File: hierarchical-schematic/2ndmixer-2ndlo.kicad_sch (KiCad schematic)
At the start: 54 parts, among them J201 110.7 MHz In, J202 Conn_01x02, J203 2nd Mixer Out, Q201 2N5179, Q202 2N5179, T201 Bifilar_Transformer, U201 MAV-11, U202 TUF-1H+, Y201 100MHz

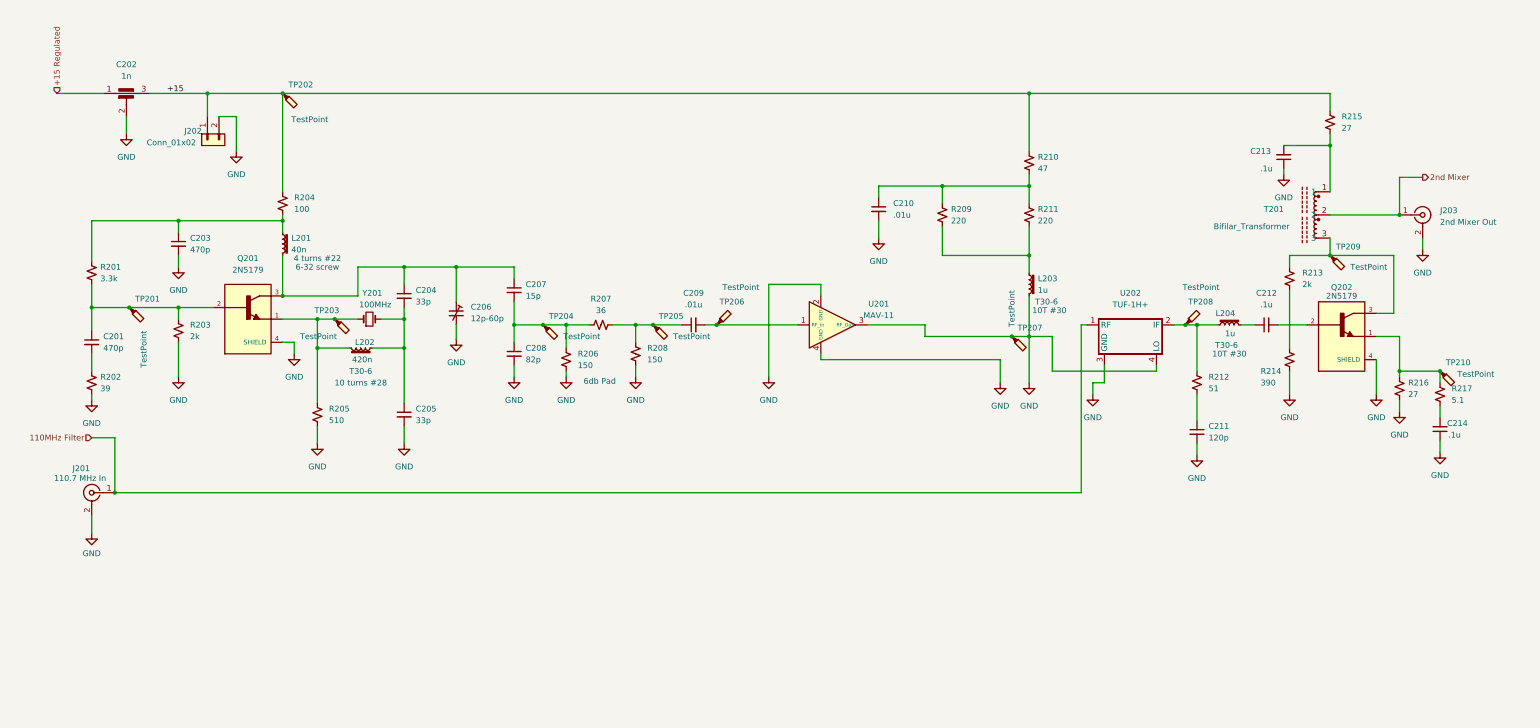
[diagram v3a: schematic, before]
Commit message: Fixes to 2ndmixer-2ndlo and vco-1stmixer
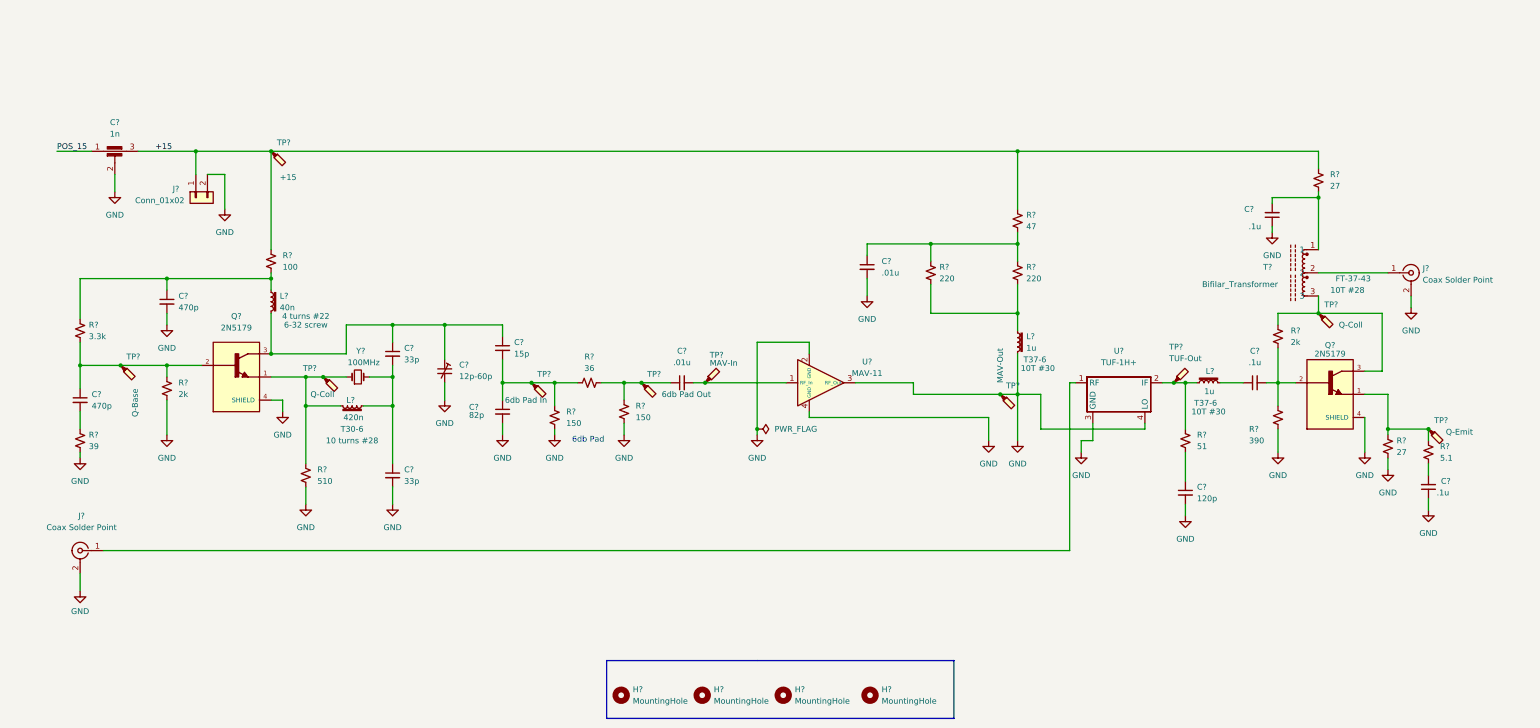
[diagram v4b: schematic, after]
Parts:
- removed C201, C203: 470p, Capacitor_THT:C_Disc_D5.0mm_W2.5mm_P5.00mm, symbol Device:C_Small
- removed C202: 1n, 2ndmixer-2ndlo:DSS1NB32A102Q91A, symbol Device:C_Feedthrough
- removed C204, C205: 33p, Capacitor_THT:C_Disc_D5.0mm_W2.5mm_P5.00mm, symbol Device:C_Small
- removed C206: 12p-60p, 2ndmixer-2ndlo:GKG60015, symbol Device:C_Trim_Small
- removed C207: 15p, Capacitor_THT:C_Disc_D5.0mm_W2.5mm_P5.00mm, symbol Device:C_Small
- removed C208: 82p, Capacitor_THT:C_Disc_D5.0mm_W2.5mm_P5.00mm, symbol Device:C_Small
- removed C209, C210: .01u, Capacitor_THT:C_Disc_D5.0mm_W2.5mm_P5.00mm, symbol Device:C_Small
- removed C211: 120p, Capacitor_THT:C_Disc_D5.0mm_W2.5mm_P5.00mm, symbol Device:C_Small
- removed C212, C213, C214: .1u, Capacitor_THT:C_Disc_D5.0mm_W2.5mm_P5.00mm, symbol Device:C_Small
- removed J201: 110.7 MHz In, Connector_Wire:SolderWire-0.5sqmm_1x02_P4.6mm_D0.9mm_OD2.1mm, symbol Connector:Conn_Coaxial
- removed J202: Conn_01x02, 2ndmixer-2ndlo:691103110002, symbol Connector_Generic:Conn_01x02
- removed J203: 2nd Mixer Out, Connector_Wire:SolderWire-0.5sqmm_1x02_P4.6mm_D0.9mm_OD2.1mm, symbol Connector:Conn_Coaxial
- removed L201: 40n, Inductor_THT:L_Toroid_Vertical_L13.0mm_W6.5mm_P5.60mm, symbol Device:L_Iron_Small
- removed L202: 420n, Inductor_THT:L_Toroid_Vertical_L13.0mm_W6.5mm_P5.60mm, symbol Device:L_Iron_Small
- removed L203, L204: 1u, Inductor_THT:L_Toroid_Vertical_L13.0mm_W6.5mm_P5.60mm, symbol Device:L_Iron_Small
- removed Q201, Q202: 2N5179, TO127P584H533-4N, symbol spectrum analyzer:2N5179
- removed R201: 3.3k, Resistor_THT:R_Axial_DIN0207_L6.3mm_D2.5mm_P7.62mm_Horizontal, symbol Device:R_Small_US
- removed R202: 39, Resistor_THT:R_Axial_DIN0207_L6.3mm_D2.5mm_P7.62mm_Horizontal, symbol Device:R_Small_US
- removed R203, R213: 2k, Resistor_THT:R_Axial_DIN0207_L6.3mm_D2.5mm_P7.62mm_Horizontal, symbol Device:R_Small_US
- removed R204: 100, Resistor_THT:R_Axial_DIN0207_L6.3mm_D2.5mm_P7.62mm_Horizontal, symbol Device:R_Small_US
- removed R205: 510, Resistor_THT:R_Axial_DIN0207_L6.3mm_D2.5mm_P7.62mm_Horizontal, symbol Device:R_Small_US
- removed R206, R208: 150, Resistor_THT:R_Axial_DIN0207_L6.3mm_D2.5mm_P7.62mm_Horizontal, symbol Device:R_Small_US
- removed R207: 36, Resistor_THT:R_Axial_DIN0207_L6.3mm_D2.5mm_P7.62mm_Horizontal, symbol Device:R_Small_US
- removed R209, R211: 220, Resistor_THT:R_Axial_DIN0207_L6.3mm_D2.5mm_P7.62mm_Horizontal, symbol Device:R_Small_US
- removed R210: 47, Resistor_THT:R_Axial_DIN0207_L6.3mm_D2.5mm_P7.62mm_Horizontal, symbol Device:R_Small_US
- removed R212: 51, Resistor_THT:R_Axial_DIN0207_L6.3mm_D2.5mm_P7.62mm_Horizontal, symbol Device:R_Small_US
- removed R214: 390, Resistor_THT:R_Axial_DIN0207_L6.3mm_D2.5mm_P7.62mm_Horizontal, symbol Device:R_Small_US
- removed R215, R216: 27, Resistor_THT:R_Axial_DIN0207_L6.3mm_D2.5mm_P7.62mm_Horizontal, symbol Device:R_Small_US
- removed R217: 5.1, Resistor_THT:R_Axial_DIN0207_L6.3mm_D2.5mm_P7.62mm_Horizontal, symbol Device:R_Small_US
- removed T201: Bifilar_Transformer, Transformer_THT:Autotransformer_Toroid_1Tap_Horizontal_D10.5mm_Amidon-T37, symbol spectrum analyzer:Bifilar_Transformer
- removed TP201, TP202, TP203, TP204, TP205, TP206, TP207, TP208, TP209, TP210: TestPoint, TestPoint:TestPoint_Pad_1.0x1.0mm, symbol Connector:TestPoint_Probe
- removed U201: MAV-11, 2ndmixer-2ndlo:MAV-11BSM&plus_, symbol spectrum analyzer:MAV-11
- removed U202: TUF-1H+, 2ndmixer-2ndlo:TUF-1H, symbol spectrum analyzer:TUF-1H+
- removed Y201: 100MHz, Crystal:Crystal_HC49-U_Vertical, symbol Device:Crystal_Small
- added C? (x3): .1u, Capacitor_THT:C_Disc_D5.0mm_W2.5mm_P5.00mm, symbol Device:C_Small
- added C?: 15p, Capacitor_THT:C_Disc_D5.0mm_W2.5mm_P5.00mm, symbol Device:C_Small
- added C?: 120p, Capacitor_THT:C_Disc_D5.0mm_W2.5mm_P5.00mm, symbol Device:C_Small
- added C? (x2): 33p, Capacitor_THT:C_Disc_D5.0mm_W2.5mm_P5.00mm, symbol Device:C_Small
- added C?: 1n, 2ndmixer-2ndlo:DSS1NB32A102Q91A, symbol Device:C_Feedthrough
- added C?: 82p, Capacitor_THT:C_Disc_D5.0mm_W2.5mm_P5.00mm, symbol Device:C_Small
- added C?: 12p-60p, 2ndmixer-2ndlo:GKG60015, symbol Device:C_Trim_Small
- added C? (x2): 470p, Capacitor_THT:C_Disc_D5.0mm_W2.5mm_P5.00mm, symbol Device:C_Small
- added C? (x2): .01u, Capacitor_THT:C_Disc_D5.0mm_W2.5mm_P5.00mm, symbol Device:C_Small
- added H? (x4): MountingHole, MountingHole:MountingHole_3.2mm_M3, symbol Mechanical:MountingHole
- added J? (x2): Coax Solder Point, Connector_Wire:SolderWire-0.5sqmm_1x02_P4.6mm_D0.9mm_OD2.1mm, symbol Connector:Conn_Coaxial
- added J?: Conn_01x02, 2ndmixer-2ndlo:691103110002, symbol Connector_Generic:Conn_01x02
- added L?: 40n, Inductor_THT:L_Toroid_Vertical_L13.0mm_W6.5mm_P5.60mm, symbol Device:L_Iron_Small
- added L?: 420n, Inductor_THT:L_Toroid_Vertical_L13.0mm_W6.5mm_P5.60mm, symbol Device:L_Iron_Small
- added L? (x2): 1u, Inductor_THT:L_Toroid_Vertical_L13.0mm_W6.5mm_P5.60mm, symbol Device:L_Iron_Small
- added Q?: 2N5179, TO127P584H533-4N, symbol spectrum_analyzer:2N5179
- added Q?: 2N5179, 2ndmixer-2ndlo:TO127P584H533-4N, symbol 2ndmixer-2ndlo:2N5179
- added R?: 100, Resistor_THT:R_Axial_DIN0207_L6.3mm_D2.5mm_P7.62mm_Horizontal, symbol Device:R_Small_US
- added R?: 47, Resistor_THT:R_Axial_DIN0207_L6.3mm_D2.5mm_P7.62mm_Horizontal, symbol Device:R_Small_US
- added R? (x2): 220, Resistor_THT:R_Axial_DIN0207_L6.3mm_D2.5mm_P7.62mm_Horizontal, symbol Device:R_Small_US
- added R? (x2): 27, Resistor_THT:R_Axial_DIN0207_L6.3mm_D2.5mm_P7.62mm_Horizontal, symbol Device:R_Small_US
- added R? (x2): 150, Resistor_THT:R_Axial_DIN0207_L6.3mm_D2.5mm_P7.62mm_Horizontal, symbol Device:R_Small_US
- added R? (x2): 2k, Resistor_THT:R_Axial_DIN0207_L6.3mm_D2.5mm_P7.62mm_Horizontal, symbol Device:R_Small_US
- added R?: 51, Resistor_THT:R_Axial_DIN0207_L6.3mm_D2.5mm_P7.62mm_Horizontal, symbol Device:R_Small_US
- added R?: 390, Resistor_THT:R_Axial_DIN0207_L6.3mm_D2.5mm_P7.62mm_Horizontal, symbol Device:R_Small_US
- added R?: 3.3k, Resistor_THT:R_Axial_DIN0207_L6.3mm_D2.5mm_P7.62mm_Horizontal, symbol Device:R_Small_US
- added R?: 36, Resistor_THT:R_Axial_DIN0207_L6.3mm_D2.5mm_P7.62mm_Horizontal, symbol Device:R_Small_US
- added R?: 510, Resistor_THT:R_Axial_DIN0207_L6.3mm_D2.5mm_P7.62mm_Horizontal, symbol Device:R_Small_US
- added R?: 39, Resistor_THT:R_Axial_DIN0207_L6.3mm_D2.5mm_P7.62mm_Horizontal, symbol Device:R_Small_US
- added R?: 5.1, Resistor_THT:R_Axial_DIN0207_L6.3mm_D2.5mm_P7.62mm_Horizontal, symbol Device:R_Small_US
- added T?: Bifilar_Transformer, Transformer_THT:Autotransformer_Toroid_1Tap_Horizontal_D10.5mm_Amidon-T37, symbol spectrum_analyzer:Bifilar_Transformer
- added TP? (x2): Q-Coll, TestPoint:TestPoint_Pad_1.0x1.0mm, symbol Connector:TestPoint_Probe
- added TP?: 6db Pad Out, TestPoint:TestPoint_Pad_1.0x1.0mm, symbol Connector:TestPoint_Probe
- added TP?: MAV-Out, TestPoint:TestPoint_Pad_1.0x1.0mm, symbol Connector:TestPoint_Probe
- added TP?: Q-Emit, TestPoint:TestPoint_Pad_1.0x1.0mm, symbol Connector:TestPoint_Probe
- added TP?: +15, TestPoint:TestPoint_Pad_1.0x1.0mm, symbol Connector:TestPoint_Probe
- added TP?: 6db Pad In, TestPoint:TestPoint_Pad_1.0x1.0mm, symbol Connector:TestPoint_Probe
- added TP?: Q-Base, TestPoint:TestPoint_Pad_1.0x1.0mm, symbol Connector:TestPoint_Probe
- added TP?: TUF-Out, TestPoint:TestPoint_Pad_1.0x1.0mm, symbol Connector:TestPoint_Probe
- added TP?: MAV-In, TestPoint:TestPoint_Pad_1.0x1.0mm, symbol Connector:TestPoint_Probe
- added U?: MAV-11, 2ndmixer-2ndlo:MAV-11BSM&plus_, symbol spectrum_analyzer:MAV-11
- added U?: TUF-1H+, 2ndmixer-2ndlo:TUF-1H, symbol spectrum_analyzer:TUF-1H+
- added Y?: 100MHz, Crystal:Crystal_HC49-U_Vertical, symbol Device:Crystal_Small
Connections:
- net +15: now also C?.3, J?.1 (Pin_1), R?.1, R?.1, R?.1, TP?.1
- net GND: now also C?.1, C?.1, C?.2, C?.2, C?.2, C?.2, C?.2, C?.2, C?.2, J?.2 (Ext), J?.2 (Ext), J?.2 (Pin_2), L?.2, Q?.4 (SHIELD), Q?.4 (SHIELD), R?.2, R?.2, R?.2, R?.2, R?.2, R?.2, R?.2, TP?.1, U?.2 (GND), U?.3 (GND), U?.3 (RF_Out), U?.4 (GND), U?.4 (LO)
- new net: C?.2, R?.2, T?.1
- new net: Q?.3, R?.1, T?.3, TP?.1
- new net: C?.1, C?.1, C?.1, L?.2, Q?.3
- new net: C?.1, C?.2, R?.1, R?.1, TP?.1
- new net: C?.1, R?.1, R?.2, TP?.1
- new net: L?.2, Q?.1, R?.1, TP?.1, Y?.1
- new net: C?.1, L?.1, R?.1, R?.2
- new net: C?.1, R?.2
- new net: C?.1, R?.1, R?.1, R?.2
- new net: C?.1, C?.2, L?.1, Y?.2
- new net: C?.1, L?.2
- new net: C?.2, Q?.2, R?.1, R?.2
- new net: L?.1, R?.2, R?.2
- new net: Q?.1, R?.1, R?.1, TP?.1
- new net: C?.2, TP?.1, U?.1 (RF_In)
- new net: J?.1 (In), T?.2
- new net: J?.1 (In), U?.1 (RF)
- new net: L?.1, R?.1, TP?.1, U?.2 (IF)
- new net: C?.1, Q?.2, R?.1, R?.2, TP?.1
- new net: C?.2, R?.2
- new net: C?.2, R?.1
- new net POS_15: C?.1
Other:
- title: (none) -> 2nd Mixer and Second LO

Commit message: v7 conversion
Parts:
- J? (x2): Spice_Model Conn_Coaxial -> (none); Spice_Netlist_Enabled N -> (none); Spice_Primitive J -> (none)
- J?: Spice_Model Conn_01x02 -> (none); Spice_Netlist_Enabled N -> (none); Spice_Primitive J -> (none)
- Q? (x2): Spice_Lib_File 2ndmixer-2ndlo-spice\2N5179.LIB -> (none); Spice_Model 2N5179 -> (none); Spice_Netlist_Enabled Y -> (none); Spice_Primitive Q -> (none)
- TP? (x2): value Q-Coll -> ${SIM.PARAMS}; Spice_Netlist_Enabled N -> (none)
- TP?: value 6db Pad Out -> ${SIM.PARAMS}; Spice_Netlist_Enabled N -> (none)
- TP?: value MAV-Out -> ${SIM.PARAMS}; Spice_Netlist_Enabled N -> (none)
- TP?: value Q-Emit -> ${SIM.PARAMS}; Spice_Netlist_Enabled N -> (none)
- TP?: value +15 -> ${SIM.PARAMS}; Spice_Netlist_Enabled N -> (none)
- TP?: value 6db Pad In -> ${SIM.PARAMS}; Spice_Netlist_Enabled N -> (none)
- TP?: value Q-Base -> ${SIM.PARAMS}; Spice_Netlist_Enabled N -> (none)
- TP?: value TUF-Out -> ${SIM.PARAMS}; Spice_Netlist_Enabled N -> (none)
- TP?: value MAV-In -> ${SIM.PARAMS}; Spice_Netlist_Enabled N -> (none)

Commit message: 2ndmixer-2ndlo rev 1
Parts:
- removed C? (x3): .1u, Capacitor_THT:C_Disc_D5.0mm_W2.5mm_P5.00mm, symbol Device:C_Small
- removed C?: 15p, Capacitor_THT:C_Disc_D5.0mm_W2.5mm_P5.00mm, symbol Device:C_Small
- removed C?: 120p, Capacitor_THT:C_Disc_D5.0mm_W2.5mm_P5.00mm, symbol Device:C_Small
- removed C? (x2): 33p, Capacitor_THT:C_Disc_D5.0mm_W2.5mm_P5.00mm, symbol Device:C_Small
- removed C?: 1n, 2ndmixer-2ndlo:DSS1NB32A102Q91A, symbol Device:C_Feedthrough
- removed C?: 82p, Capacitor_THT:C_Disc_D5.0mm_W2.5mm_P5.00mm, symbol Device:C_Small
- removed C?: 12p-60p, 2ndmixer-2ndlo:GKG60015, symbol Device:C_Trim_Small
- removed C? (x2): 470p, Capacitor_THT:C_Disc_D5.0mm_W2.5mm_P5.00mm, symbol Device:C_Small
- removed C? (x2): .01u, Capacitor_THT:C_Disc_D5.0mm_W2.5mm_P5.00mm, symbol Device:C_Small
- removed H? (x4): MountingHole, MountingHole:MountingHole_3.2mm_M3, symbol Mechanical:MountingHole
- removed J? (x2): Coax Solder Point, Connector_Wire:SolderWire-0.5sqmm_1x02_P4.6mm_D0.9mm_OD2.1mm, symbol Connector:Conn_Coaxial
- removed J?: Conn_01x02, 2ndmixer-2ndlo:691103110002, symbol Connector_Generic:Conn_01x02
- removed L?: 40n, Inductor_THT:L_Toroid_Vertical_L13.0mm_W6.5mm_P5.60mm, symbol Device:L_Iron_Small
- removed L?: 420n, Inductor_THT:L_Toroid_Vertical_L13.0mm_W6.5mm_P5.60mm, symbol Device:L_Iron_Small
- removed L? (x2): 1u, Inductor_THT:L_Toroid_Vertical_L13.0mm_W6.5mm_P5.60mm, symbol Device:L_Iron_Small
- removed Q?: 2N5179, TO127P584H533-4N, symbol spectrum_analyzer:2N5179
- removed Q?: 2N5179, 2ndmixer-2ndlo:TO127P584H533-4N, symbol 2ndmixer-2ndlo:2N5179
- removed R?: 100, Resistor_THT:R_Axial_DIN0207_L6.3mm_D2.5mm_P7.62mm_Horizontal, symbol Device:R_Small_US
- removed R?: 47, Resistor_THT:R_Axial_DIN0207_L6.3mm_D2.5mm_P7.62mm_Horizontal, symbol Device:R_Small_US
- removed R? (x2): 220, Resistor_THT:R_Axial_DIN0207_L6.3mm_D2.5mm_P7.62mm_Horizontal, symbol Device:R_Small_US
- removed R? (x2): 27, Resistor_THT:R_Axial_DIN0207_L6.3mm_D2.5mm_P7.62mm_Horizontal, symbol Device:R_Small_US
- removed R? (x2): 150, Resistor_THT:R_Axial_DIN0207_L6.3mm_D2.5mm_P7.62mm_Horizontal, symbol Device:R_Small_US
- removed R? (x2): 2k, Resistor_THT:R_Axial_DIN0207_L6.3mm_D2.5mm_P7.62mm_Horizontal, symbol Device:R_Small_US
- removed R?: 51, Resistor_THT:R_Axial_DIN0207_L6.3mm_D2.5mm_P7.62mm_Horizontal, symbol Device:R_Small_US
- removed R?: 390, Resistor_THT:R_Axial_DIN0207_L6.3mm_D2.5mm_P7.62mm_Horizontal, symbol Device:R_Small_US
- removed R?: 3.3k, Resistor_THT:R_Axial_DIN0207_L6.3mm_D2.5mm_P7.62mm_Horizontal, symbol Device:R_Small_US
- removed R?: 36, Resistor_THT:R_Axial_DIN0207_L6.3mm_D2.5mm_P7.62mm_Horizontal, symbol Device:R_Small_US
- removed R?: 510, Resistor_THT:R_Axial_DIN0207_L6.3mm_D2.5mm_P7.62mm_Horizontal, symbol Device:R_Small_US
- removed R?: 39, Resistor_THT:R_Axial_DIN0207_L6.3mm_D2.5mm_P7.62mm_Horizontal, symbol Device:R_Small_US
- removed R?: 5.1, Resistor_THT:R_Axial_DIN0207_L6.3mm_D2.5mm_P7.62mm_Horizontal, symbol Device:R_Small_US
- removed T?: Bifilar_Transformer, Transformer_THT:Autotransformer_Toroid_1Tap_Horizontal_D10.5mm_Amidon-T37, symbol spectrum_analyzer:Bifilar_Transformer
- removed TP? (x10): ${SIM.PARAMS}, TestPoint:TestPoint_Pad_1.0x1.0mm, symbol Connector:TestPoint_Probe
- removed U?: MAV-11, 2ndmixer-2ndlo:MAV-11BSM&plus_, symbol spectrum_analyzer:MAV-11
- removed U?: TUF-1H+, 2ndmixer-2ndlo:TUF-1H, symbol spectrum_analyzer:TUF-1H+
- removed Y?: 100MHz, Crystal:Crystal_HC49-U_Vertical, symbol Device:Crystal_Small
- added C1201, C1203: 470p, Capacitor_THT:C_Disc_D5.0mm_W2.5mm_P5.00mm, symbol Device:C_Small
- added C1202: 1n, spectrum_analyzer:DSS1NB32A102Q91A, symbol Device:C_Feedthrough
- added C1204, C1205: 33p, Capacitor_THT:C_Disc_D5.0mm_W2.5mm_P5.00mm, symbol Device:C_Small
- added C1206: 12p-60p, spectrum_analyzer:GKG60015, symbol Device:C_Trim_Small
- added C1207: 15p, Capacitor_THT:C_Disc_D5.0mm_W2.5mm_P5.00mm, symbol Device:C_Small
- added C1208: 82p, Capacitor_THT:C_Disc_D5.0mm_W2.5mm_P5.00mm, symbol Device:C_Small
- added C1209, C1210: .01u, Capacitor_THT:C_Disc_D5.0mm_W2.5mm_P5.00mm, symbol Device:C_Small
- added C1211: 120p, Capacitor_THT:C_Disc_D5.0mm_W2.5mm_P5.00mm, symbol Device:C_Small
- added C1212, C1213, C1214: .1u, Capacitor_THT:C_Disc_D5.0mm_W2.5mm_P5.00mm, symbol Device:C_Small
- added H1201, H1202, H1203, H1204: MountingHole, MountingHole:MountingHole_3.2mm_M3, symbol Mechanical:MountingHole
- added J1201, J1203: Coax Solder Point, Connector_Wire:SolderWire-0.5sqmm_1x02_P4.6mm_D0.9mm_OD2.1mm, symbol Connector:Conn_Coaxial
- added J1202: Conn_01x02, spectrum_analyzer:691103110002, symbol Connector_Generic:Conn_01x02
- added L1201: 40n, Inductor_THT:L_Toroid_Vertical_L13.0mm_W6.5mm_P5.60mm, symbol Device:L_Iron_Small
- added L1202: 420n, Inductor_THT:L_Toroid_Vertical_L13.0mm_W6.5mm_P5.60mm, symbol Device:L_Iron_Small
- added L1203, L1204: 1u, Inductor_THT:L_Toroid_Vertical_L13.0mm_W6.5mm_P5.60mm, symbol Device:L_Iron_Small
- added Q1201: 2N5179, spectrum_analyzer:TO127P584H533-4N, symbol spectrum_analyzer:2N5179
- added Q1202: 2N5179, TO127P584H533-4N, symbol spectrum_analyzer:2N5179
- added R1201: 3.3k, Resistor_THT:R_Axial_DIN0207_L6.3mm_D2.5mm_P7.62mm_Horizontal, symbol Device:R_Small_US
- added R1202: 39, Resistor_THT:R_Axial_DIN0207_L6.3mm_D2.5mm_P7.62mm_Horizontal, symbol Device:R_Small_US
- added R1203, R1213: 2k, Resistor_THT:R_Axial_DIN0207_L6.3mm_D2.5mm_P7.62mm_Horizontal, symbol Device:R_Small_US
- added R1204: 100, Resistor_THT:R_Axial_DIN0207_L6.3mm_D2.5mm_P7.62mm_Horizontal, symbol Device:R_Small_US
- added R1205: 510, Resistor_THT:R_Axial_DIN0207_L6.3mm_D2.5mm_P7.62mm_Horizontal, symbol Device:R_Small_US
- added R1206, R1208: 150, Resistor_THT:R_Axial_DIN0207_L6.3mm_D2.5mm_P7.62mm_Horizontal, symbol Device:R_Small_US
- added R1207: 36, Resistor_THT:R_Axial_DIN0207_L6.3mm_D2.5mm_P7.62mm_Horizontal, symbol Device:R_Small_US
- added R1209, R1211: 220, Resistor_THT:R_Axial_DIN0207_L6.3mm_D2.5mm_P7.62mm_Horizontal, symbol Device:R_Small_US
- added R1210: 47, Resistor_THT:R_Axial_DIN0207_L6.3mm_D2.5mm_P7.62mm_Horizontal, symbol Device:R_Small_US
- added R1212: 51, Resistor_THT:R_Axial_DIN0207_L6.3mm_D2.5mm_P7.62mm_Horizontal, symbol Device:R_Small_US
- added R1214: 390, Resistor_THT:R_Axial_DIN0207_L6.3mm_D2.5mm_P7.62mm_Horizontal, symbol Device:R_Small_US
- added R1215, R1216: 27, Resistor_THT:R_Axial_DIN0207_L6.3mm_D2.5mm_P7.62mm_Horizontal, symbol Device:R_Small_US
- added R1217: 5.1, Resistor_THT:R_Axial_DIN0207_L6.3mm_D2.5mm_P7.62mm_Horizontal, symbol Device:R_Small_US
- added T1201: Bifilar_Transformer, Transformer_THT:Autotransformer_Toroid_1Tap_Horizontal_D10.5mm_Amidon-T37, symbol spectrum_analyzer:Bifilar_Transformer
- added TP1201: Q-Base1, TestPoint:TestPoint_Pad_1.0x1.0mm, symbol Connector:TestPoint_Probe
- added TP1202: +15, TestPoint:TestPoint_Pad_1.0x1.0mm, symbol Connector:TestPoint_Probe
- added TP1203: Q-Emit1, TestPoint:TestPoint_Pad_1.0x1.0mm, symbol Connector:TestPoint_Probe
- added TP1204: Q-Coll1, TestPoint:TestPoint_Pad_1.0x1.0mm, symbol Connector:TestPoint_Probe
- added TP1205: 6db Pad In, TestPoint:TestPoint_Pad_1.0x1.0mm, symbol Connector:TestPoint_Probe
- added TP1206: 6db Pad Out, TestPoint:TestPoint_Pad_1.0x1.0mm, symbol Connector:TestPoint_Probe
- added TP1207: MAV-In, TestPoint:TestPoint_Pad_1.0x1.0mm, symbol Connector:TestPoint_Probe
- added TP1208: MAV-Out, TestPoint:TestPoint_Pad_1.0x1.0mm, symbol Connector:TestPoint_Probe
- added TP1209: TUF-Out, TestPoint:TestPoint_Pad_1.0x1.0mm, symbol Connector:TestPoint_Probe
- added TP1210: Q-Base2, TestPoint:TestPoint_Pad_1.0x1.0mm, symbol Connector:TestPoint_Probe
- added TP1211: Q-Coll2, TestPoint:TestPoint_Pad_1.0x1.0mm, symbol Connector:TestPoint_Probe
- added TP1212: Q-Emit2, TestPoint:TestPoint_Pad_1.0x1.0mm, symbol Connector:TestPoint_Probe
- added U1201: MAV-11, spectrum_analyzer:MAV-11BSM&plus_, symbol spectrum_analyzer:MAV-11
- added U1202: TUF-1H+, spectrum_analyzer:TUF-1H, symbol spectrum_analyzer:TUF-1H+
- added Y1201: 100MHz, Crystal:Crystal_HC49-U_Vertical, symbol Device:Crystal_Small
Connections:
- net +15: now also C1202.3, J1202.1 (Pin_1), R1204.1, R1210.1, R1215.1, TP1202.1
- net GND: now also C1202.2, C1203.2, C1205.2, C1206.2, C1208.2, C1210.2, C1211.2, C1213.1, C1214.1, J1201.2 (Ext), J1202.2 (Pin_2), J1203.2 (Ext), L1203.2, Q1201.4 (SHIELD), Q1202.4 (SHIELD), R1202.2, R1203.2, R1205.2, R1206.2, R1208.2, R1214.2, R1216.2, TP1208.1, U1201.2 (GND), U1201.3 (RF_Out), U1201.4 (GND), U1202.3 (GND), U1202.4 (LO)
- new net: J1201.1 (In), U1202.1 (RF)
- new net: L1204.1, R1212.1, TP1209.1, U1202.2 (IF)
- new net: C1210.1, R1209.1, R1210.2, R1211.1
- new net: C1209.2, TP1207.1, U1201.1 (RF_In)
- new net: C1204.2, C1205.1, L1202.1, Y1201.2
- new net: L1202.2, Q1201.1, R1205.1, TP1204.1, Y1201.1
- new net: Q1202.3, R1213.1, T1201.3, TP1211.1
- new net: C1212.2, Q1202.2, R1213.2, R1214.1, TP1210.1
- new net: C1209.1, R1207.2, R1208.1, TP1206.1
- new net: C1214.2, R1217.2
- new net: L1203.1, R1209.2, R1211.2
- new net: C1212.1, L1204.2
- new net: C1203.1, L1201.1, R1201.1, R1204.2
- new net: C1201.1, Q1201.2, R1201.2, R1203.1, TP1201.1
- new net: C1204.1, C1206.1, C1207.1, L1201.2, Q1201.3, TP1203.1
- new net: C1207.2, C1208.1, R1206.1, R1207.1, TP1205.1
- new net: C1201.2, R1202.1
- new net: C1213.2, R1215.2, T1201.1
- new net: C1211.1, R1212.2
- new net: Q1202.1, R1216.1, R1217.1, TP1212.1
- new net +15 Regulated: C1202.1
- new net 2nd Mixer: J1203.1 (In), T1201.2
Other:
- note added: "http://www.kangaus.com/documentation/New%20SA/Second_LO_SCH.pdf"
